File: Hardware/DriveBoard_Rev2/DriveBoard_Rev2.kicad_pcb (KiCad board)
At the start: 2 copper layers, 152.4 x 101.6 mm, 139 parts, among them J1 RJ45_LED_Shielded, Q1 Q_NMOS_DGS, Q2 Q_NMOS_DGS, Q3 Q_NMOS_DGS, Q4 Q_NMOS_DGS, Q5 Q_NMOS_DGS, Q6 Q_NMOS_DGS, Q7 Q_NMOS_DGS, Q8 Q_NMOS_DGS, Q9 Q_NMOS_DGS, SW1 SW_Push, SW10 SW_Push, SW11 SW_Push, SW12 SW_Push, SW13 SW_Push, SW14 SW_Push, SW15 SW_Push, SW16 SW_SPDT, SW2 SW_Push, SW3 SW_Push, SW4 SW_Push, SW5 SW_Push, SW6 SW_Push, SW7 SW_Push, SW8 SW_Push, SW9 SW_Push, U1 Teensy4.1_DEV-16771, U2 TSR_1-2450, U3 OKI, U4 74HC148, U5 74HC148, U6 74HC00, U7 TSR_1-2450

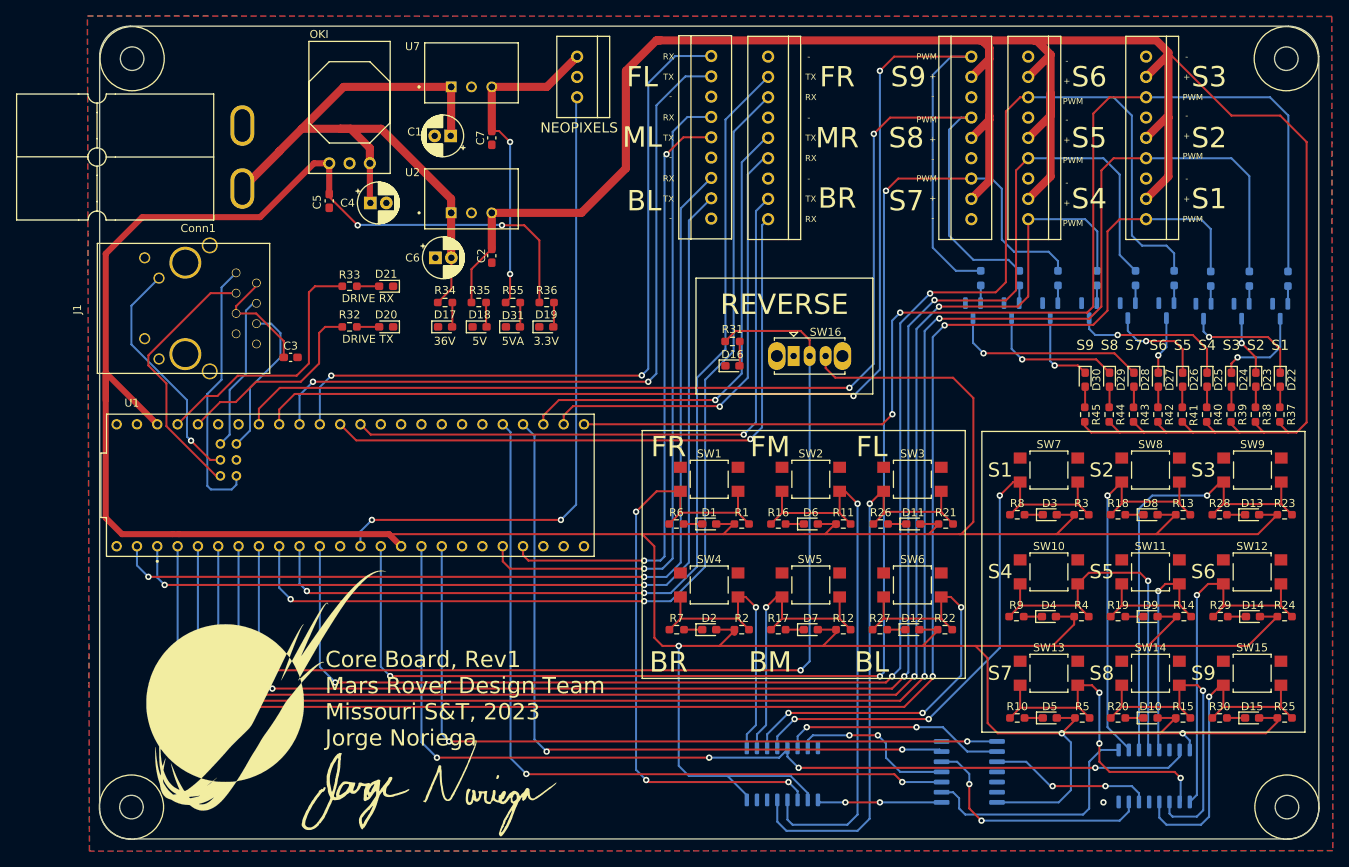
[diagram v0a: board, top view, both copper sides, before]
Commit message: PCB Layout Core Board
Finished
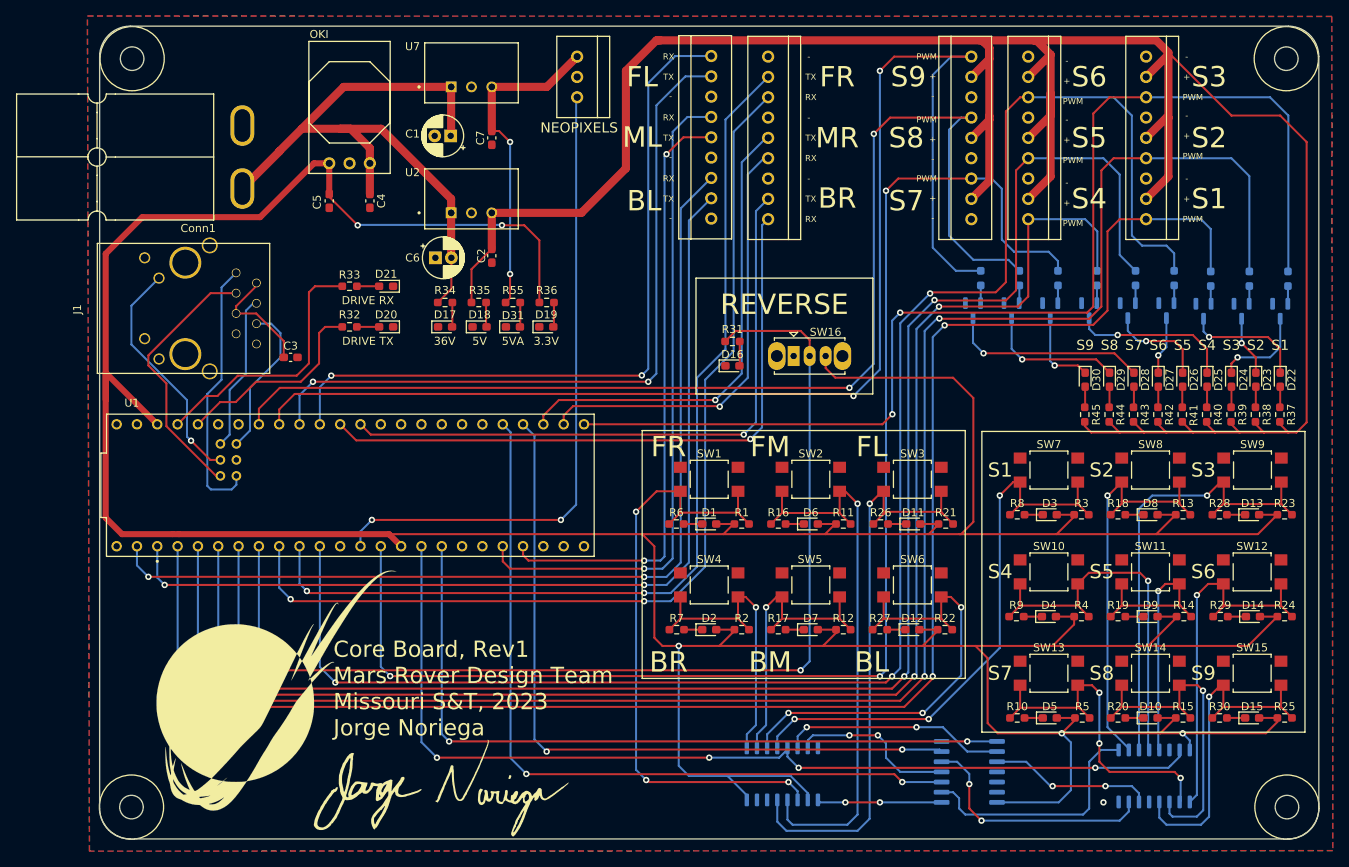
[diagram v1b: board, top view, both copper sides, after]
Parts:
- C4: footprint Capacitor_THT:CP_Radial_D5.0mm_P2.00mm -> Capacitor_SMD:C_0603_1608Metric_Pad1.08x0.95mm_HandSolder
- moved G*** 1.52 mm to (73.9, 134.1)
- moved G*** 1.27 mm to (53.8, 121.2)
- moved C4 0.26 mm to (65.5, 59.9), turned to -90 degrees
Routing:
- net +36V: track 85.0 -> 83.8 mm
- net +3V3: track 578.5 -> 577.5 mm

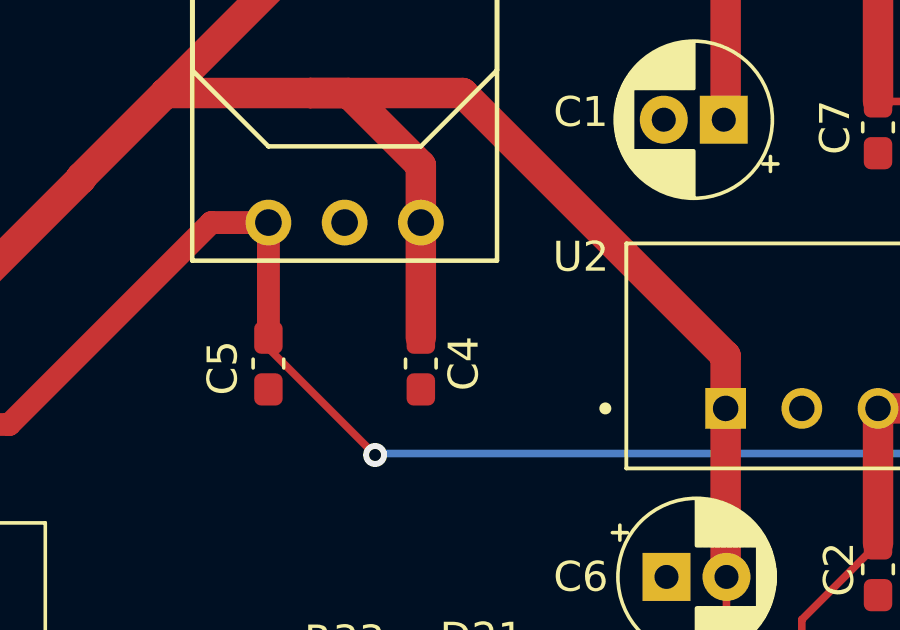
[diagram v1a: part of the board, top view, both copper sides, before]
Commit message: Corrected Capacitor
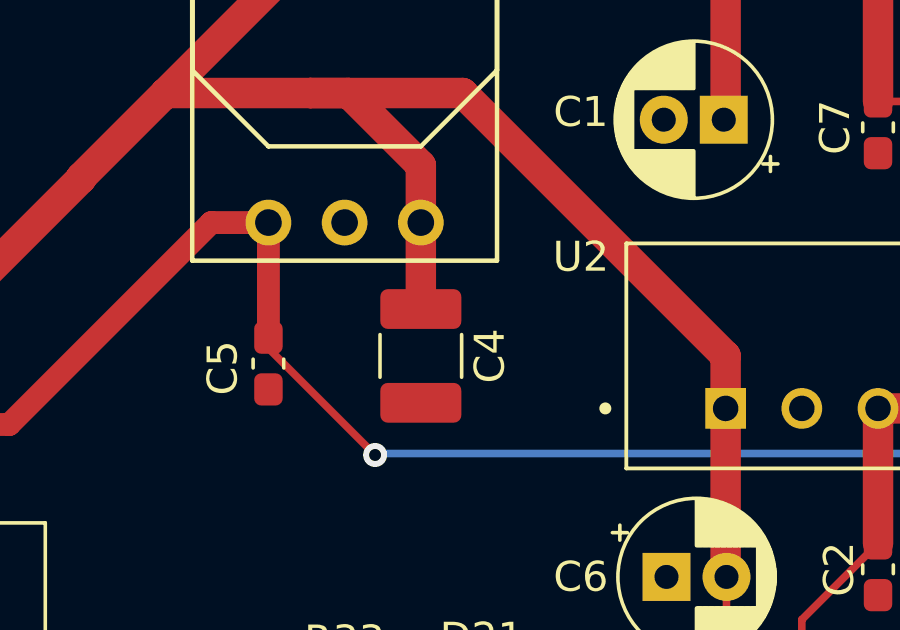
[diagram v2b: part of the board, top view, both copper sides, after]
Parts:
- C4: footprint Capacitor_SMD:C_0603_1608Metric_Pad1.08x0.95mm_HandSolder -> Capacitor_SMD:C_1210_3225Metric_Pad1.33x2.70mm_HandSolder
- moved C4 0.25 mm to (65.5, 59.7)
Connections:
- U1 pad R-: /RX- -> (no net)
- U1 pad T-: /TX- -> (no net)
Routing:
- net +36V: track 83.8 -> 82.9 mm
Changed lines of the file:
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@@
     )
   )
-  (footprint "Capacitor_SMD:C_0603_1608Metric_Pad1.08x0.95mm_HandSolder" (layer "F.Cu")
-    (at 65.532 59.944 -90)
-    (descr "Capacitor SMD 0603 (1608 Metric), square (rectangular) end terminal, IPC_7351 nominal with elongated pad for handsoldering. (Body size source: IPC-SM-782 page 76, https://www.pcb-3d.com/wordpress/wp-content/uploads/ipc-sm-782a_amendment_1_and_2.pdf), generated with kicad-footprint-generator")
-    (tags "capacitor handsolder")
-    (property "Sheetfile" "DriveBoard_Rev2.kicad_sch")
-    (property "Sheetname" "")
-    (attr smd)
-    (fp_text reference "C4" (at 0 -1.43 90) (layer "F.SilkS")
-      (effects (font (size 1 1) (thickness 0.15)))
-    )
-    (fp_text value "10uF" (at 0 1.43 90) (layer "F.Fab")
-      (effects (font (size 1 1) (thickness 0.15)))
-    )
-    (fp_text user "${REFERENCE}" (at 0 0 90) (layer "F.Fab")
-      (effects (font (size 0.4 0.4) (thickness 0.06)))
-    )
-    (fp_line (start -0.146267 -0.51) (end 0.146267 -0.51) (layer "F.SilkS") (width 0.12))
-    (fp_line (start -0.146267 0.51) (end 0.146267 0.51) (layer "F.SilkS") (width 0.12))
-    (fp_line (start 1.65 0.73) (end -1.65 0.73) (layer "F.CrtYd") (width 0.05))
-    (fp_line (start -1.65 -0.73) (end 1.65 -0.73) (layer "F.CrtYd") (width 0.05))
-    (fp_line (start 1.65 -0.73) (end 1.65 0.73) (layer "F.CrtYd") (width 0.05))
-    (fp_line (start -1.65 0.73) (end -1.65 -0.73) (layer "F.CrtYd") (width 0.05))
-    (fp_line (start -0.8 -0.4) (end 0.8 -0.4) (layer "F.Fab") (width 0.1))
-    (fp_line (start 0.8 -0.4) (end 0.8 0.4) (layer "F.Fab") (width 0.1))
-    (fp_line (start -0.8 0.4) (end -0.8 -0.4) (layer "F.Fab") (width 0.1))
-    (fp_line (start 0.8 0.4) (end -0.8 0.4) (layer "F.Fab") (width 0.1))
-    (pad "1" smd roundrect (at -0.8625 0 270) (size 1.075 0.95) (layers "F.Cu" "F.Paste" "F.Mask") (roundrect_rratio 0.25)
-      (net 1 "+36V") (pintype "passive"))
-    (pad "2" smd roundrect (at 0.8625 0 270) (size 1.075 0.95) (layers "F.Cu" "F.Paste" "F.Mask") (roundrect_rratio 0.25)
-      (net 2 "GND") (pintype "passive"))
-    (model "${KICAD6_3DMODEL_DIR}/Capacitor_SMD.3dshapes/C_0603_1608Metric.wrl"
-      (offset (xyz 0 0 0))
-      (scale (xyz 1 1 1))
-      (rotate (xyz 0 0 0))
-    )
-  )
   (footprint "Capacitor_THT:CP_Radial_D5.0mm_P2.00mm" (layer "F.Cu")
     (at 75.631113 51.816 180)
@@
     (pad "R+" thru_hole circle (at -16.24 -5.17) (size 1.208 1.208) (drill 0.7) (layers *.Cu *.Mask)
       (net 81 "/RX+") (pinfunction "R+") (pintype "bidirectional"))
-    (pad "R-" thru_hole circle (at -14.24 -5.17) (size 1.208 1.208) (drill 0.7) (layers *.Cu *.Mask)
-      (net 118 "/RX-"))
+    (pad "R-" thru_hole circle (at -14.24 -5.17) (size 1.208 1.208) (drill 0.7) (layers *.Cu *.Mask))
     (pad "T+" thru_hole circle (at -14.24 -1.17) (size 1.208 1.208) (drill 0.7) (layers *.Cu *.Mask)
       (net 79 "/TX+") (pinfunction "T+") (pintype "bidirectional"))
-    (pad "T-" thru_hole circle (at -16.24 -1.17) (size 1.208 1.208) (drill 0.7) (layers *.Cu *.Mask)
-      (net 80 "/TX-"))
+    (pad "T-" thru_hole circle (at -16.24 -1.17) (size 1.208 1.208) (drill 0.7) (layers *.Cu *.Mask))
     (pad "VIN" thru_hole circle (at -29.21 -7.62) (size 1.308 1.308) (drill 0.8) (layers *.Cu *.Mask)
       (net 74 "unconnected-(U1-PadVIN)") (pinfunction "VIN") (pintype "input+no_connect"))
@@
     )
   )
+  (footprint "Capacitor_SMD:C_1210_3225Metric_Pad1.33x2.70mm_HandSolder" (layer "F.Cu")
+    (at 65.532 59.69 -90)
+    (descr "Capacitor SMD 1210 (3225 Metric), square (rectangular) end terminal, IPC_7351 nominal with elongated pad for handsoldering. (Body size source: IPC-SM-782 page 76, https://www.pcb-3d.com/wordpress/wp-content/uploads/ipc-sm-782a_amendment_1_and_2.pdf), generated with kicad-footprint-generator")
+    (tags "capacitor handsolder")
+    (property "Sheetfile" "DriveBoard_Rev2.kicad_sch")
+    (property "Sheetname" "")
+    (attr smd)
+    (fp_text reference "C4" (at 0 -2.3 90) (layer "F.SilkS")
+      (effects (font (size 1 1) (thickness 0.15)))
+    )
+    (fp_text value "10uF" (at 0 2.3 90) (layer "F.Fab")
+      (effects (font (size 1 1) (thickness 0.15)))
+    )
+    (fp_text user "${REFERENCE}" (at 0 0 90) (layer "F.Fab")
+      (effects (font (size 0.8 0.8) (thickness 0.12)))
+    )
+    (fp_line (start -0.711252 1.36) (end 0.711252 1.36) (layer "F.SilkS") (width 0.12))
+    (fp_line (start -0.711252 -1.36) (end 0.711252 -1.36) (layer "F.SilkS") (width 0.12))
+    (fp_line (start -2.48 -1.6) (end 2.48 -1.6) (layer "F.CrtYd") (width 0.05))
+    (fp_line (start 2.48 1.6) (end -2.48 1.6) (layer "F.CrtYd") (width 0.05))
+    (fp_line (start 2.48 -1.6) (end 2.48 1.6) (layer "F.CrtYd") (width 0.05))
+    (fp_line (start -2.48 1.6) (end -2.48 -1.6) (layer "F.CrtYd") (width 0.05))
+    (fp_line (start -1.6 1.25) (end -1.6 -1.25) (layer "F.Fab") (width 0.1))
+    (fp_line (start 1.6 -1.25) (end 1.6 1.25) (layer "F.Fab") (width 0.1))
+    (fp_line (start -1.6 -1.25) (end 1.6 -1.25) (layer "F.Fab") (width 0.1))
+    (fp_line (start 1.6 1.25) (end -1.6 1.25) (layer "F.Fab") (width 0.1))
+    (pad "1" smd roundrect (at -1.5625 0 270) (size 1.325 2.7) (layers "F.Cu" "F.Paste" "F.Mask") (roundrect_rratio 0.188679)
+      (net 1 "+36V") (pintype "passive"))
+    (pad "2" smd roundrect (at 1.5625 0 270) (size 1.325 2.7) (layers "F.Cu" "F.Paste" "F.Mask") (roundrect_rratio 0.188679)
+      (net 2 "GND") (pintype "passive"))
+    (model "${KICAD6_3DMODEL_DIR}/Capacitor_SMD.3dshapes/C_1210_3225Metric.wrl"
+      (offset (xyz 0 0 0))
+      (scale (xyz 1 1 1))
+      (rotate (xyz 0 0 0))
+    )
+  )
   (footprint "Button_Switch_SMD:SW_SPST_TL3305A" (layer "F.Cu")
     (at 150.415 106.318)
@@
   )
   (segment (start 75.692 61.44) (end 75.692 67.027112) (width 1.016) (layer "F.Cu") (net 1))
+  (segment (start 65.532 55.245) (end 65.532 58.1275) (width 1.016) (layer "F.Cu") (net 1))
   (segment (start 54.2122 53.775) (end 54.2122 53.7378) (width 1.016) (layer "F.Cu") (net 1))
   (segment (start 54.2122 53.7378) (end 57.023 50.927) (width 1.016) (layer "F.Cu") (net 1))
@@
   (segment (start 61.849 50.927) (end 63.119 50.927) (width 1.016) (layer "F.Cu") (net 1))
   (segment (start 57.023 50.927) (end 62.258 45.692) (width 1.016) (layer "F.Cu") (net 1))
-  (segment (start 65.532 55.245) (end 65.532 59.0815) (width 1.016) (layer "F.Cu") (net 1))
   (segment (start 66.929 50.927) (end 61.849 50.927) (width 1.016) (layer "F.Cu") (net 1))
   (segment (start 65.532 53.34) (end 63.119 50.927) (width 1.016) (layer "F.Cu") (net 1))
